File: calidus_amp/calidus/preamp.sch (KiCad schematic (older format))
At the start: 20 parts

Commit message: Daily update
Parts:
- removed U? (x3): NE5532, symbol Amplifier_Operational:NE5532
- added C? (x2): 220p, symbol Device:C
- added R? (x2): 100, symbol Device:R
- added U? (x3): OPA2134, symbol Amplifier_Operational:OPA2134
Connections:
- net GNDS: now also C?.1, C?.2
- net at C?.1, R?.1: now also U?.6 (-)
- net at C?.2, R?.2: now also U?.5 (+)
- net at C?.1, C?.1, R?.1: now also U?.7
- net at C?.1, C?.1, R?.1: now also U?.1
- net at C?.2, R?.2: now also U?.2 (-)
- net at C?.2, R?.2: now also R?.1; no longer C?.2
- net at C?.1, R?.2: now also U?.3 (+)
- net at C?.1, R?.2: now also R?.1; no longer C?.2
- net our_r renamed potout_r
- net out_l renamed potout_l
- new net: C?.2, C?.2, R?.2
- new net: C?.1, C?.2, R?.2
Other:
- moved on the sheet: C?, R?

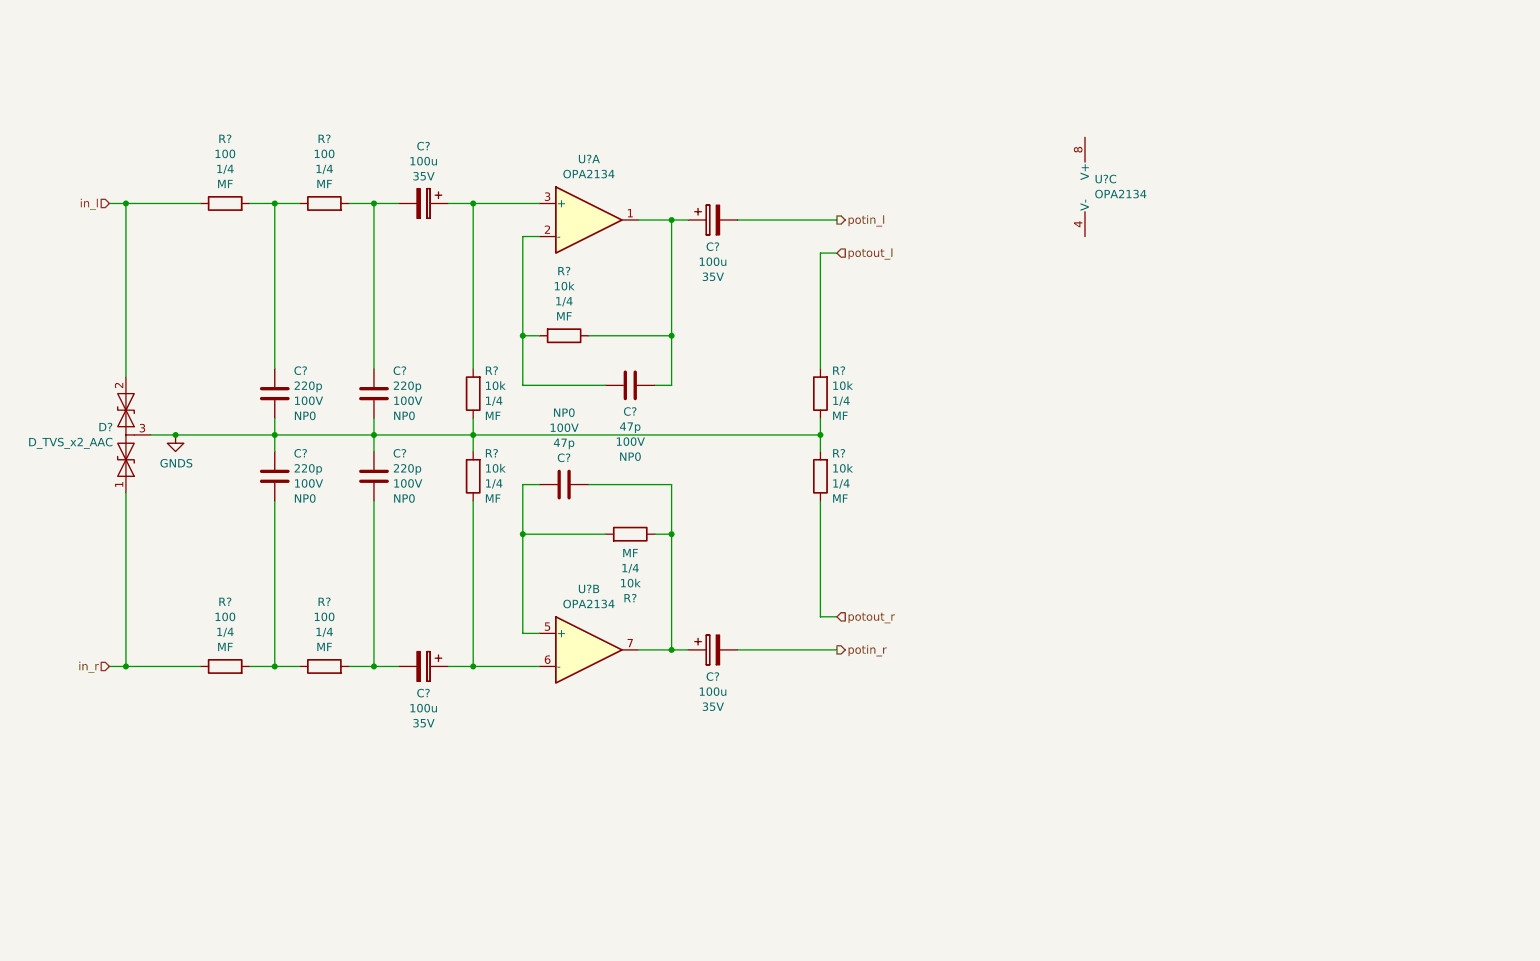
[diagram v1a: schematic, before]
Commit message: Updated component designators and finished CMU
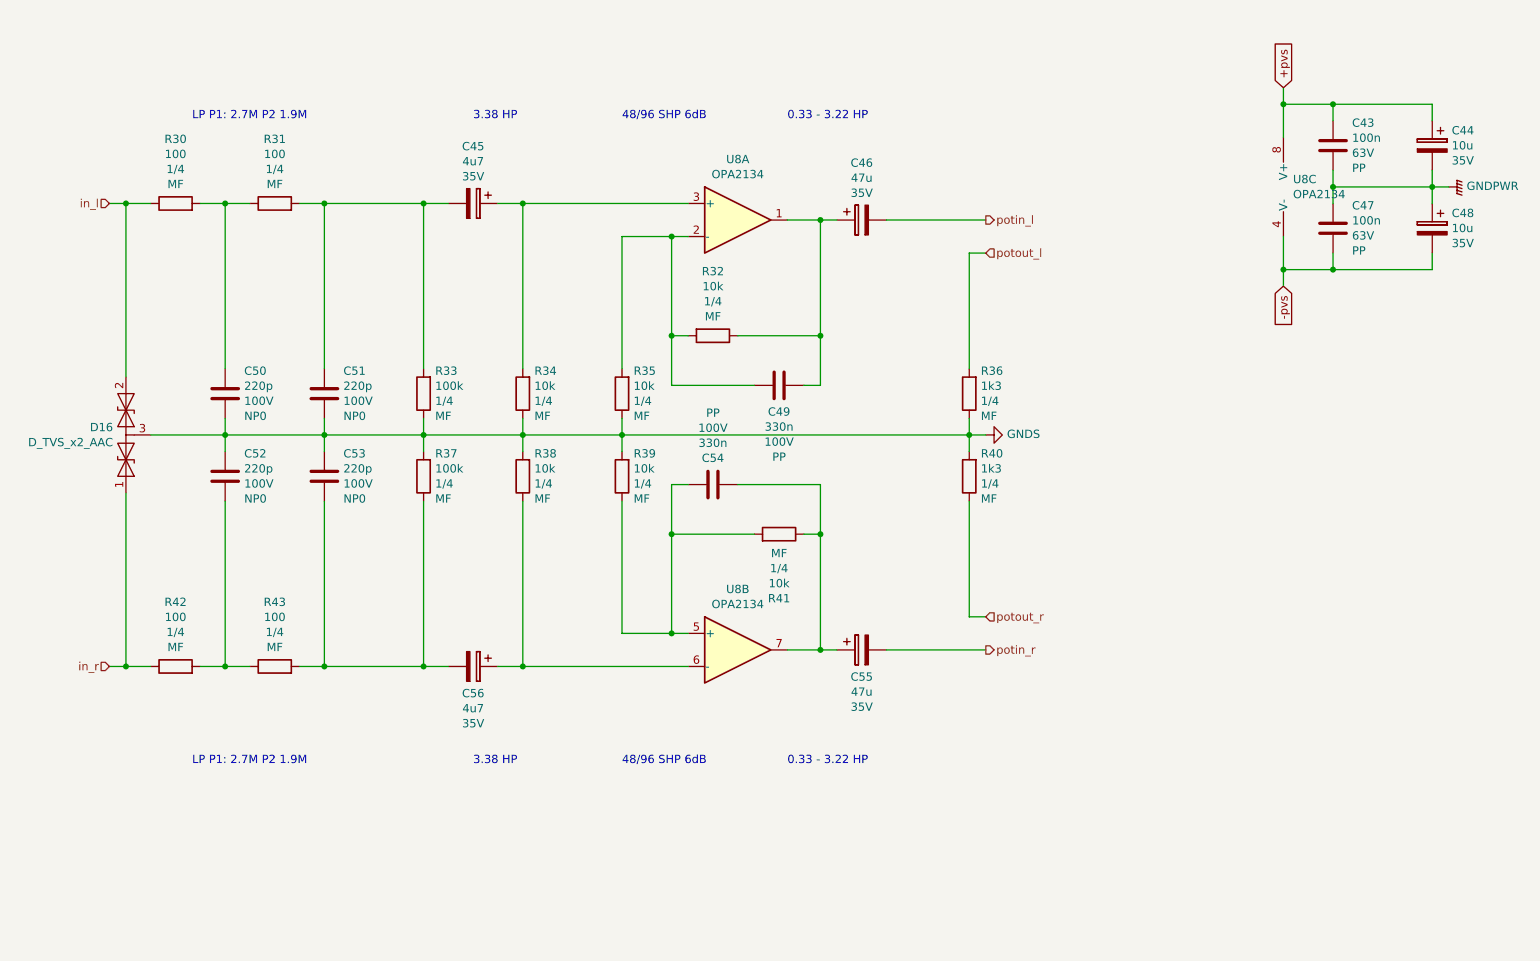
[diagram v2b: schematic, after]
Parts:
- added C43, C47: 100n, symbol Device:C
- added C44, C48: 10u, symbol Device:CP
- added R33, R37: 100k, symbol Device:R
- added R35, R39: 10k, symbol Device:R
- C45, C56: renamed from C?; value 100u -> 4u7
- C46, C55: renamed from C?; value 100u -> 47u
- C49, C54: renamed from C?; value 47p -> 330n; Type NP0 -> PP
- R36, R40: renamed from R?; value 10k -> 1k3
- U8: renamed from U?; footprint (none) -> Package_DIP:DIP-8_W7.62mm_LongPads
- gave numbers to parts that had none: 13
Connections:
- net GNDS: now also R33.1, R35.1, R37.2, R39.2
- net at C49.2, R32.2, U8.2 (-): now also R35.2
- net at C53.2, C56.2, R43.2: now also R37.1
- net at C54.2, R41.2, U8.5 (+): now also R39.1
- net at C45.2, C51.1, R31.2: now also R33.2
- net -pvs: now reaches U8.4 (V-)
- net -pvs: now also C47.2, C48.2
- net +pvs: now reaches U8.8 (V+)
- net +pvs: now also C43.1, C44.1
- new net GNDPWR: C43.2, C44.2, C47.1, C48.1
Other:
- note added: "0.33 - 3.22 HP"
- note added: "3.38 HP"
- note added: "48/96 SHP 6dB"
- note added: "LP P1: 2.7M P2 1.9M"
- moved on the sheet: C45, C46, C49, C50, C51, C52, C53, C54, C55, C56, R30, R31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

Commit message: Updated schematic and footprinted Rybicon capacitors
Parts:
- removed C44, C48: 10u, symbol Device:CP
- removed C46, C55: 47u, symbol Device:CP
- removed C56: 4u7, symbol Device:CP
- added C? (x2): 10u, Capacitor_THT:CP_Radial_D5.0mm_P2.00mm, symbol Device:CP
- added C?: 4u7, Capacitor_THT:CP_Radial_D5.0mm_P2.00mm, symbol Device:CP
- added C? (x2): 47u, Capacitor_THT:CP_Radial_D6.3mm_P2.50mm, symbol Device:CP
- C45: footprint (none) -> Capacitor_THT:CP_Radial_D5.0mm_P2.00mm; Manufacturer (none) -> Rybicon:50YXF4R7MEFC5X11; Supplier1 (none) -> Farnell:2811491; Voltage 35V -> 50V
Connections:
- net +pvs: now also C?.1
- net -pvs: now also C?.2
- net GNDPWR: now also C?.1, C?.2
- net potin_l: now also C?.2
- net potin_r: now also C?.2
- net at C49.1, R32.1, U8.1: now also C?.1
- net at R38.1, U8.6 (-): now also C?.1
- net at C53.2, R37.1, R43.2: now also C?.2
- net at C54.1, R41.1, U8.7: now also C?.1
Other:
- note added: "Place the capacitors as\nclose as possible to IC\npins"
- moved on the sheet: U8C
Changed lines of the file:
@@
 F 0 "C45" V 3655 2500 50  0000 C CNN
 F 1 "4u7" V 3746 2500 50  0000 C CNN
-F 2 "" H 4038 2350 50  0001 C CNN
-F 3 "~" H 4000 2500 50  0001 C CNN
-F 4 "35V" V 3837 2500 50  0000 C CNN "Voltage"
+F 2 "Capacitor_THT:CP_Radial_D5.0mm_P2.00mm" H 4038 2350 50  0001 C CNN
+F 3 "http://www.farnell.com/datasheets/2321304.pdf" H 4000 2500 50  0001 C CNN
+F 4 "50V" V 3837 2500 50  0000 C CNN "Voltage"
+F 5 "Rybicon:50YXF4R7MEFC5X11" V 4000 2500 50  0001 C CNN "Manufacturer"
+F 6 "Farnell:2811491" V 4000 2500 50  0001 C CNN "Supplier1"
 	1    4000 2500
 	0    1    1    0
@@
 Wire Wire Line
 	4300 4300 4300 5300
-$Comp
-L Device:CP C56
-U 1 1 5C4215F5
-P 4000 5300
-F 0 "C56" V 4163 5300 50  0000 C CNN
-F 1 "4u7" V 4254 5300 50  0000 C CNN
-F 2 "" H 4038 5150 50  0001 C CNN
-F 3 "~" H 4000 5300 50  0001 C CNN
-F 4 "35V" V 4345 5300 50  0000 C CNN "Voltage"
-	1    4000 5300
-	0    1    1    0
-$EndComp
 Text HLabel 7100 5200 2    50   Output ~ 0
 potin_r
@@
 	6100 5200 6200 5200
 $Comp
-L Device:CP C55
-U 1 1 5C435076
-P 6350 5200
-F 0 "C55" V 6513 5200 50  0000 C CNN
-F 1 "47u" V 6604 5200 50  0000 C CNN
-F 2 "" H 6388 5050 50  0001 C CNN
-F 3 "~" H 6350 5200 50  0001 C CNN
-F 4 "35V" V 6695 5200 50  0000 C CNN "Voltage"
-	1    6350 5200
-	0    -1   1    0
-$EndComp
-$Comp
-L Device:CP C46
-U 1 1 5C42D4B4
-P 6350 2600
-F 0 "C46" V 6005 2600 50  0000 C CNN
-F 1 "47u" V 6096 2600 50  0000 C CNN
-F 2 "" H 6388 2450 50  0001 C CNN
-F 3 "~" H 6350 2600 50  0001 C CNN
-F 4 "35V" V 6187 2600 50  0000 C CNN "Voltage"
-	1    6350 2600
-	0    -1   1    0
-$EndComp
-$Comp
 L Amplifier_Operational:OPA2134 U8
 U 1 1 5C47C2F3
@@
 L Amplifier_Operational:OPA2134 U8
 U 3 1 5C47C4ED
-P 9000 2400
-F 0 "U8" H 8958 2446 50  0000 L CNN
-F 1 "OPA2134" H 8958 2355 50  0000 L CNN
-F 2 "Package_DIP:DIP-8_W7.62mm_LongPads" H 9000 2400 50  0001 C CNN
-F 3 "http://www.ti.com/lit/ds/symlink/opa134.pdf" H 9000 2400 50  0001 C CNN
-	3    9000 2400
+P 8700 2400
+F 0 "U8" H 8658 2446 50  0000 L CNN
+F 1 "OPA2134" H 8658 2355 50  0000 L CNN
+F 2 "Package_DIP:DIP-8_W7.62mm_LongPads" H 8700 2400 50  0001 C CNN
+F 3 "http://www.ti.com/lit/ds/symlink/opa134.pdf" H 8700 2400 50  0001 C CNN
+	3    8700 2400
 	1    0    0    -1
 $EndComp
@@
 Wire Wire Line
 	3700 4300 3700 5300
-Text GLabel 8900 1800 1    50   Input ~ 0
+Text GLabel 8600 1800 1    50   Input ~ 0
 +pvs
-Text GLabel 8900 3000 3    50   Input ~ 0
+Text GLabel 8600 3000 3    50   Input ~ 0
 -pvs
 Wire Wire Line
-	8900 2100 8900 1900
-Wire Wire Line
-	8900 3000 8900 2900
+	8600 2100 8600 1900
+Wire Wire Line
+	8600 3000 8600 2900
 $Comp
 L power:GNDPWR #PWR030
@@
 $EndComp
 Wire Wire Line
-	8900 2900 9200 2900
+	8600 2900 9200 2900
 Wire Wire Line
 	9200 2900 9200 2800
 Wire Wire Line
-	8900 1900 9200 1900
+	8600 1900 9200 1900
 Wire Wire Line
 	9200 1900 9200 2000
@@
 Wire Wire Line
 	9200 2300 9200 2400
-Connection ~ 8900 1900
-Wire Wire Line
-	8900 1900 8900 1800
-Connection ~ 8900 2900
-Wire Wire Line
-	8900 2900 8900 2700
+Connection ~ 8600 1900
+Wire Wire Line
+	8600 1900 8600 1800
+Connection ~ 8600 2900
+Wire Wire Line
+	8600 2900 8600 2700
 Wire Wire Line
 	9900 2400 9800 2400
@@
 	9800 2900 9200 2900
 Connection ~ 9200 2900
-$Comp
-L Device:CP C44
-U 1 1 5C577B9E
+Wire Wire Line
+	9800 2300 9800 2400
+Wire Wire Line
+	9800 2800 9800 2900
+Text Notes 8900 1600 0    50   ~ 0
+Place the capacitors as\nclose as possible to IC\npins
+$Comp
+L Device:CP C?
+U 1 1 5C5A5B6F
 P 9800 2150
-F 0 "C44" H 9682 2241 50  0000 R CNN
+AR Path="/5C37BC48/5C5A5B6F" Ref="C?"  Part="1"
+AR Path="/5C4751C0/5C5A5B6F" Ref="C?"  Part="1"
+F 0 "C?" H 9682 2241 50  0000 R CNN
 F 1 "10u" H 9682 2150 50  0000 R CNN
-F 2 "" H 9838 2000 50  0001 C CNN
-F 3 "~" H 9800 2150 50  0001 C CNN
-F 4 "35V" H 9682 2059 50  0000 R CNN "Voltage"
+F 2 "Capacitor_THT:CP_Radial_D5.0mm_P2.00mm" H 9838 2000 50  0001 C CNN
+F 3 "http://www.farnell.com/datasheets/2124421.pdf" H 9800 2150 50  0001 C CNN
+F 4 "50V" H 9682 2059 50  0000 R CNN "Voltage"
+F 5 "Rybicon:50YXF10MEFC5X11" H 9800 2150 50  0001 C CNN "Manufacturer"
+F 6 "Farnell:1144632" H 9800 2150 50  0001 C CNN "Supplier1"
 	1    9800 2150
 	-1   0    0    -1
 $EndComp
-Wire Wire Line
-	9800 2300 9800 2400
-$Comp
-L Device:CP C48
-U 1 1 5C577EB0
+$Comp
+L Device:CP C?
+U 1 1 5C5A7F98
 P 9800 2650
-F 0 "C48" H 9682 2741 50  0000 R CNN
+AR Path="/5C37BC48/5C5A7F98" Ref="C?"  Part="1"
+AR Path="/5C4751C0/5C5A7F98" Ref="C?"  Part="1"
+F 0 "C?" H 9682 2741 50  0000 R CNN
 F 1 "10u" H 9682 2650 50  0000 R CNN
-F 2 "" H 9838 2500 50  0001 C CNN
-F 3 "~" H 9800 2650 50  0001 C CNN
-F 4 "35V" H 9682 2559 50  0000 R CNN "Voltage"
+F 2 "Capacitor_THT:CP_Radial_D5.0mm_P2.00mm" H 9838 2500 50  0001 C CNN
+F 3 "http://www.farnell.com/datasheets/2124421.pdf" H 9800 2650 50  0001 C CNN
+F 4 "50V" H 9682 2559 50  0000 R CNN "Voltage"
+F 5 "Rybicon:50YXF10MEFC5X11" H 9800 2650 50  0001 C CNN "Manufacturer"
+F 6 "Farnell:1144632" H 9800 2650 50  0001 C CNN "Supplier1"
 	1    9800 2650
 	-1   0    0    -1
 $EndComp
-Wire Wire Line
-	9800 2800 9800 2900
+$Comp
+L Device:CP C?
+U 1 1 5C5AD364
+P 4000 5300
+F 0 "C?" V 3655 5300 50  0000 C CNN
+F 1 "4u7" V 3746 5300 50  0000 C CNN
+F 2 "Capacitor_THT:CP_Radial_D5.0mm_P2.00mm" H 4038 5150 50  0001 C CNN
+F 3 "http://www.farnell.com/datasheets/2321304.pdf" H 4000 5300 50  0001 C CNN
+F 4 "50V" V 3837 5300 50  0000 C CNN "Voltage"
+F 5 "Rybicon:50YXF4R7MEFC5X11" V 4000 5300 50  0001 C CNN "Manufacturer"
+F 6 "Farnell:2811491" V 4000 5300 50  0001 C CNN "Supplier1"
+	1    4000 5300
+	0    1    1    0
+$EndComp
+$Comp
+L Device:CP C?
+U 1 1 5C5B02C7
+P 6350 2600
+AR Path="/5C37BC7C/5C5B02C7" Ref="C?"  Part="1"
+AR Path="/5C4751C0/5C5B02C7" Ref="C?"  Part="1"
+F 0 "C?" V 6005 2600 50  0000 C CNN
+F 1 "47u" V 6096 2600 50  0000 C CNN
+F 2 "Capacitor_THT:CP_Radial_D6.3mm_P2.50mm" H 6388 2450 50  0001 C CNN
+F 3 "http://www.farnell.com/datasheets/2321304.pdf" H 6350 2600 50  0001 C CNN
+F 4 "35V" V 6187 2600 50  0000 C CNN "Voltage"
+F 5 "Rybicon:35YXF47MEFC6.3X11" H 6350 2600 50  0001 C CNN "Manufacturer"
+F 6 "Farnell:1144626" H 6350 2600 50  0001 C CNN "Supplier1"
+	1    6350 2600
+	0    -1   1    0
+$EndComp
+$Comp
+L Device:CP C?
+U 1 1 5C5B28EB
+P 6350 5200
+AR Path="/5C37BC7C/5C5B28EB" Ref="C?"  Part="1"
+AR Path="/5C4751C0/5C5B28EB" Ref="C?"  Part="1"
+F 0 "C?" V 6005 5200 50  0000 C CNN
+F 1 "47u" V 6096 5200 50  0000 C CNN
+F 2 "Capacitor_THT:CP_Radial_D6.3mm_P2.50mm" H 6388 5050 50  0001 C CNN
+F 3 "http://www.farnell.com/datasheets/2321304.pdf" H 6350 5200 50  0001 C CNN
+F 4 "35V" V 6187 5200 50  0000 C CNN "Voltage"
+F 5 "Rybicon:35YXF47MEFC6.3X11" H 6350 5200 50  0001 C CNN "Manufacturer"
+F 6 "Farnell:1144626" H 6350 5200 50  0001 C CNN "Supplier1"
+	1    6350 5200
+	0    -1   1    0
+$EndComp
 $EndSCHEMATC
